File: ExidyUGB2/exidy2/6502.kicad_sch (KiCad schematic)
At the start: 51 parts, among them U13C NEC_UPD2114, U1A_ 74LS241, U2A UM6502, U2C_ 74LS07, U3A 74LS241, U3B 74LS241, U3C 74LS245, U3D_ 74LS00, U4C 74LS245, U4D_ 74LS04, U5C 6301, U5D 74LS138, U5E_ 74LS08

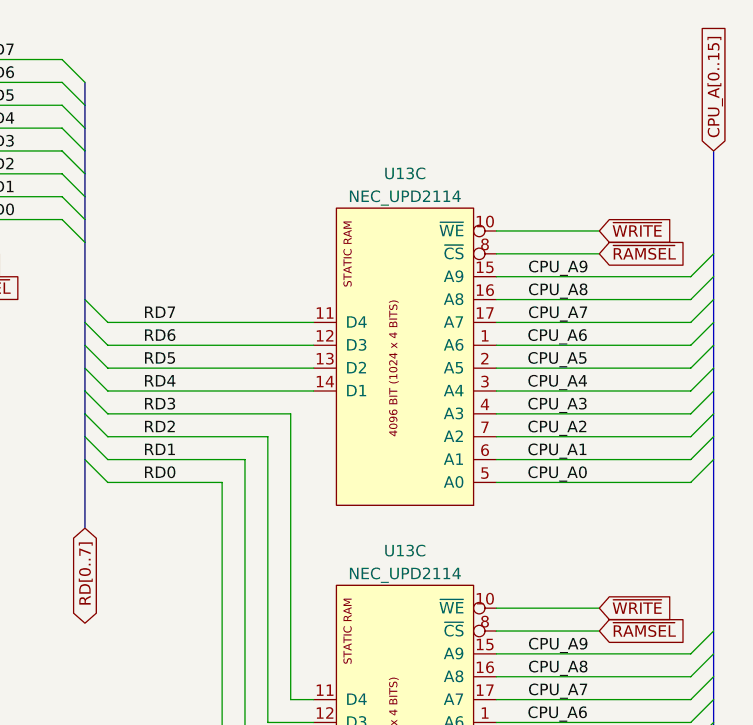
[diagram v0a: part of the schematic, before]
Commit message: Updates to KiCAD8
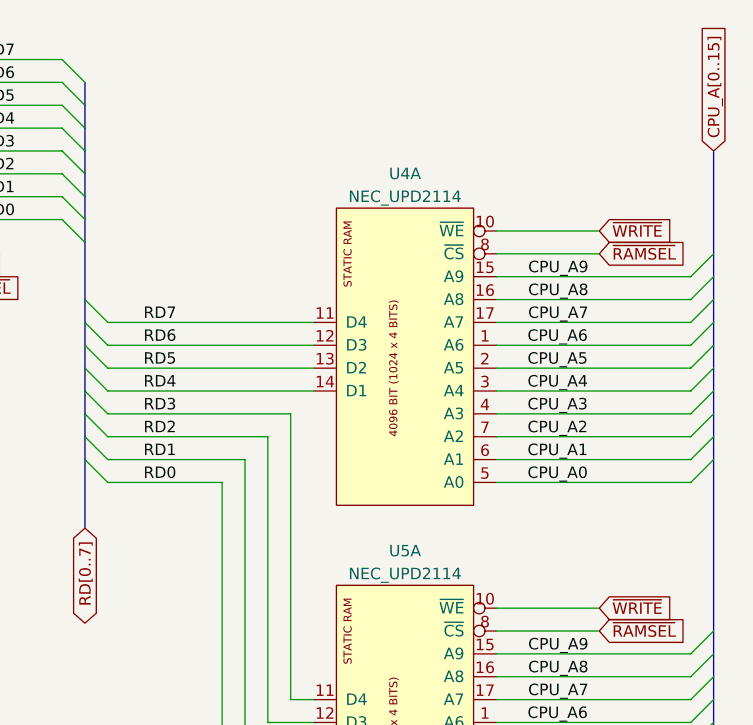
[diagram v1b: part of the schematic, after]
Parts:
- renumbered U13C to U4A, U13C to U5A
